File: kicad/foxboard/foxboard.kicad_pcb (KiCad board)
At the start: 2 copper layers, 356.7 x 159.4 mm, 183 parts, among them J2 USB_C_Receptacle_USB2.0, K1 KEYSW, K10 KEYSW, K11 KEYSW, K12 KEYSW, K13 KEYSW, K14 KEYSW, K15 KEYSW, K16 KEYSW, K17 KEYSW, K18 KEYSW, K19 KEYSW, K2 KEYSW, K20 KEYSW, K21 KEYSW, K22 KEYSW, K23 KEYSW, K24 KEYSW, K25 KEYSW, K26 KEYSW, K27 KEYSW, K28 KEYSW, K29 KEYSW, K3 KEYSW, K30 KEYSW, K31 KEYSW, K32 KEYSW, K33 KEYSW, K34 KEYSW, K35 KEYSW, K36 KEYSW, K37 KEYSW, K38 KEYSW, K39 KEYSW, K4 KEYSW, K40 KEYSW, K41 KEYSW, K42 KEYSW, K43 KEYSW, K44 KEYSW, K45 KEYSW, K46 KEYSW, K47 KEYSW, K48 KEYSW, K49 KEYSW, K5 KEYSW, K50 KEYSW, K51 KEYSW, K52 KEYSW, K53 KEYSW, K54 KEYSW, K55 KEYSW, K56 KEYSW, K57 KEYSW, K58 KEYSW, K59 KEYSW, K6 KEYSW, K60 KEYSW, K61 KEYSW, K62 KEYSW, K63 KEYSW, K64 KEYSW, K65 KEYSW, K66 KEYSW, K67 KEYSW, K68 KEYSW, K69 KEYSW, K7 KEYSW, K70 KEYSW, K71 KEYSW, K72 KEYSW, K73 KEYSW, K74 KEYSW, K75 KEYSW, K76 KEYSW, K77 KEYSW, K78 KEYSW, K79 KEYSW, K8 KEYSW, K80 KEYSW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

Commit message: move all resitors, caps and diodes to the back of the pcb
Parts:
- C3, C4, C5, C6, C7, D1, D10, D11, D12, D13, D14, D15, D16, D17, D18, D19, D2, D20, D22, D23, D24, D25, D26, D27, D28, D29, D3, D30, D31, D32, D33, D34, D35, D36, D37, D38, D39, D4, D40, D41, D42, D43, D44, D45, D46, D47, D48, D49, D5, D50, D51, D52, D53, D54, D55, D56, D57, D58, D59, D6, D60, D61, D62, D63, D64, D65, D66, D67, D68, D69, D7, D70, D71, D72, D73, D74, D75, D76, D77, D78, D79, D8, D80, D81, D82, D83, D84, D85, D86, D87, D9, R5, R6: moved to B.Cu
- moved D68 28.5 mm to (243.1, 259.5), turned to 180 degrees
- moved D87 23.4 mm to (272.5, 259.6), turned to 180 degrees
- moved D69 21.1 mm to (294.3, 259.6), turned to 180 degrees
- moved D54 20.4 mm to (315.0, 278.3), turned to 180 degrees
- moved D70 20.1 mm to (313.7, 259.7), turned to 180 degrees
- moved D52 19.9 mm to (277.4, 278.2), turned to 180 degrees
- moved D53 18.5 mm to (298.2, 278.3), turned to 180 degrees
- moved D58 16.7 mm to (48.5, 259.4), turned to 180 degrees
- moved D60 16.5 mm to (86.4, 259.3), turned to 180 degrees
- moved D65 16.5 mm to (182.8, 259.3), turned to 180 degrees
- moved D55 16.2 mm to (-8.40, 259.3), turned to 180 degrees
- moved D57 16.2 mm to (29.7, 259.4), turned to 180 degrees
- moved D59 16.2 mm to (68.0, 259.4), turned to 180 degrees
- moved D61 16.2 mm to (106.5, 259.4), turned to 180 degrees
- moved D56 16.0 mm to (11.0, 259.4), turned to 180 degrees
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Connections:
- K1 pad 1: Net-(K1-Pad1) -> Net-(U2-39_MISO1_OUT1A)
- K10 pad 1: Net-(K10-Pad1) -> Net-(U2-1_TX1_CTX2_MISO1)
- K11 pad 1: Net-(K11-Pad1) -> Net-(U2-0_RX1_CRX2_CS1)
- K13 pad 1: Net-(K13-Pad1) -> Net-(U2-40_A16)
- K14 pad 1: Net-(K14-Pad1) -> Net-(U2-41_A17)
- K15 pad 1: Net-(K15-Pad1) -> Net-(U2-13_SCK_LED)
- K16 pad 1: Net-(K16-Pad1) -> Net-(U2-14_A0_TX3_SPDIF_OUT)
- K17 pad 1: Net-(K17-Pad1) -> Net-(U2-15_A1_RX3_SPDIF_IN)
- K18 pad 1: Net-(K18-Pad1) -> Net-(U2-16_A2_RX4_SCL1)
- K19 pad 1: Net-(K19-Pad1) -> Net-(U2-17_A3_TX4_SDA1)
- K2 pad 1: Net-(K13-Pad1) -> Net-(U2-40_A16)
- K20 pad 1: Net-(K20-Pad1) -> Net-(U2-8_TX2_IN1)
- K21 pad 1: Net-(K21-Pad1) -> Net-(U2-7_RX2_OUT1A)
- K22 pad 1: Net-(K22-Pad1) -> Net-(U2-6_OUT1D)
- K24 pad 1: Net-(K10-Pad1) -> Net-(U2-1_TX1_CTX2_MISO1)
- K25 pad 1: Net-(K1-Pad1) -> Net-(U2-39_MISO1_OUT1A)
- K26 pad 1: Net-(K13-Pad1) -> Net-(U2-40_A16)
- K27 pad 1: Net-(K14-Pad1) -> Net-(U2-41_A17)
- K28 pad 1: Net-(K15-Pad1) -> Net-(U2-13_SCK_LED)
- K29 pad 1: Net-(K16-Pad1) -> Net-(U2-14_A0_TX3_SPDIF_OUT)
- K3 pad 1: Net-(K14-Pad1) -> Net-(U2-41_A17)
- K30 pad 1: Net-(K17-Pad1) -> Net-(U2-15_A1_RX3_SPDIF_IN)
- K31 pad 1: Net-(K18-Pad1) -> Net-(U2-16_A2_RX4_SCL1)
- K32 pad 1: Net-(K19-Pad1) -> Net-(U2-17_A3_TX4_SDA1)
- K33 pad 1: Net-(K20-Pad1) -> Net-(U2-8_TX2_IN1)
- K34 pad 1: Net-(K21-Pad1) -> Net-(U2-7_RX2_OUT1A)
- K35 pad 1: Net-(K22-Pad1) -> Net-(U2-6_OUT1D)
- K38 pad 1: Net-(K13-Pad1) -> Net-(U2-40_A16)
- K39 pad 1: Net-(K14-Pad1) -> Net-(U2-41_A17)
- K40 pad 1: Net-(K15-Pad1) -> Net-(U2-13_SCK_LED)
- K41 pad 1: Net-(K16-Pad1) -> Net-(U2-14_A0_TX3_SPDIF_OUT)
- K42 pad 1: Net-(K17-Pad1) -> Net-(U2-15_A1_RX3_SPDIF_IN)
- K43 pad 1: Net-(K18-Pad1) -> Net-(U2-16_A2_RX4_SCL1)
- K44 pad 1: Net-(K19-Pad1) -> Net-(U2-17_A3_TX4_SDA1)
- K45 pad 1: Net-(K20-Pad1) -> Net-(U2-8_TX2_IN1)
- K46 pad 1: Net-(K21-Pad1) -> Net-(U2-7_RX2_OUT1A)
- K48 pad 1: Net-(K22-Pad1) -> Net-(U2-6_OUT1D)
- K5 pad 1: Net-(K20-Pad1) -> Net-(U2-8_TX2_IN1)
- K51 pad 1: Net-(K51-Pad1) -> Net-(U2-2_OUT2)
- K52 pad 1: Net-(K10-Pad1) -> Net-(U2-1_TX1_CTX2_MISO1)
- K53 pad 1: Net-(K11-Pad1) -> Net-(U2-0_RX1_CRX2_CS1)
- K54 pad 1: Net-(K1-Pad1) -> Net-(U2-39_MISO1_OUT1A)
- K55 pad 1: Net-(K13-Pad1) -> Net-(U2-40_A16)
- K56 pad 1: Net-(K14-Pad1) -> Net-(U2-41_A17)
- K57 pad 1: Net-(K15-Pad1) -> Net-(U2-13_SCK_LED)
- K58 pad 1: Net-(K16-Pad1) -> Net-(U2-14_A0_TX3_SPDIF_OUT)
- K59 pad 1: Net-(K17-Pad1) -> Net-(U2-15_A1_RX3_SPDIF_IN)
- K6 pad 1: Net-(K21-Pad1) -> Net-(U2-7_RX2_OUT1A)
- K60 pad 1: Net-(K18-Pad1) -> Net-(U2-16_A2_RX4_SCL1)
- K61 pad 1: Net-(K19-Pad1) -> Net-(U2-17_A3_TX4_SDA1)
- K62 pad 1: Net-(K20-Pad1) -> Net-(U2-8_TX2_IN1)
- K63 pad 1: Net-(K21-Pad1) -> Net-(U2-7_RX2_OUT1A)
- K65 pad 1: Net-(K22-Pad1) -> Net-(U2-6_OUT1D)
- K68 pad 1: Net-(K68-Pad1) -> Net-(U2-3_LRCLK2)
- K7 pad 1: Net-(K22-Pad1) -> Net-(U2-6_OUT1D)
- K70 pad 1: Net-(K11-Pad1) -> Net-(U2-0_RX1_CRX2_CS1)
- K71 pad 1: Net-(K1-Pad1) -> Net-(U2-39_MISO1_OUT1A)
- K72 pad 1: Net-(K13-Pad1) -> Net-(U2-40_A16)
- K73 pad 1: Net-(K14-Pad1) -> Net-(U2-41_A17)
- K74 pad 1: Net-(K16-Pad1) -> Net-(U2-14_A0_TX3_SPDIF_OUT)
- K75 pad 1: Net-(K17-Pad1) -> Net-(U2-15_A1_RX3_SPDIF_IN)
- K76 pad 1: Net-(K18-Pad1) -> Net-(U2-16_A2_RX4_SCL1)
- K77 pad 1: Net-(K19-Pad1) -> Net-(U2-17_A3_TX4_SDA1)
- K78 pad 1: Net-(K20-Pad1) -> Net-(U2-8_TX2_IN1)
- K79 pad 1: Net-(K21-Pad1) -> Net-(U2-7_RX2_OUT1A)
- K80 pad 1: Net-(K22-Pad1) -> Net-(U2-6_OUT1D)
- K81 pad 1: unconnected-(K81-Pad1) -> Net-(U2-5_IN2)
- K82 pad 1: unconnected-(K82-Pad1) -> Net-(U2-4_BCLK2)
- K83 pad 1: Net-(K68-Pad1) -> Net-(U2-3_LRCLK2)
- K84 pad 1: Net-(K51-Pad1) -> Net-(U2-2_OUT2)
- K85 pad 1: Net-(K10-Pad1) -> Net-(U2-1_TX1_CTX2_MISO1)
- K86 pad 1: Net-(K11-Pad1) -> Net-(U2-0_RX1_CRX2_CS1)
- K87 pad 1: Net-(K51-Pad1) -> Net-(U2-2_OUT2)
- K9 pad 1: Net-(K51-Pad1) -> Net-(U2-2_OUT2)
- U2 pad 10: unconnected-(U2-8_TX2_IN1-Pad10) -> Net-(U2-8_TX2_IN1)
- U2 pad 2: unconnected-(U2-0_RX1_CRX2_CS1-Pad2) -> Net-(U2-0_RX1_CRX2_CS1)
- U2 pad 25: unconnected-(U2-33_MCLK2-Pad25) -> Net-(D1-K)
- U2 pad 26: unconnected-(U2-34_RX8-Pad26) -> Net-(D12-K)
- U2 pad 27: unconnected-(U2-35_TX8-Pad27) -> Net-(D25-K)
- U2 pad 28: unconnected-(U2-36_CS-Pad28) -> Net-(D37-K)
- U2 pad 29: unconnected-(U2-37_CS-Pad29) -> Net-(D54-K)
- U2 pad 3: unconnected-(U2-1_TX1_CTX2_MISO1-Pad3) -> Net-(U2-1_TX1_CTX2_MISO1)
- U2 pad 30: unconnected-(U2-38_CS1_IN1-Pad30) -> Net-(D71-K)
- U2 pad 31: unconnected-(U2-39_MISO1_OUT1A-Pad31) -> Net-(U2-39_MISO1_OUT1A)
- U2 pad 32: unconnected-(U2-40_A16-Pad32) -> Net-(U2-40_A16)
- U2 pad 33: unconnected-(U2-41_A17-Pad33) -> Net-(U2-41_A17)
- U2 pad 35: unconnected-(U2-13_SCK_LED-Pad35) -> Net-(U2-13_SCK_LED)
- U2 pad 36: unconnected-(U2-14_A0_TX3_SPDIF_OUT-Pad36) -> Net-(U2-14_A0_TX3_SPDIF_OUT)
- U2 pad 37: unconnected-(U2-15_A1_RX3_SPDIF_IN-Pad37) -> Net-(U2-15_A1_RX3_SPDIF_IN)
- U2 pad 38: unconnected-(U2-16_A2_RX4_SCL1-Pad38) -> Net-(U2-16_A2_RX4_SCL1)
- U2 pad 39: unconnected-(U2-17_A3_TX4_SDA1-Pad39) -> Net-(U2-17_A3_TX4_SDA1)
- U2 pad 4: unconnected-(U2-2_OUT2-Pad4) -> Net-(U2-2_OUT2)
- U2 pad 5: unconnected-(U2-3_LRCLK2-Pad5) -> Net-(U2-3_LRCLK2)
- U2 pad 6: unconnected-(U2-4_BCLK2-Pad6) -> Net-(U2-4_BCLK2)
- U2 pad 7: unconnected-(U2-5_IN2-Pad7) -> Net-(U2-5_IN2)
- U2 pad 8: unconnected-(U2-6_OUT1D-Pad8) -> Net-(U2-6_OUT1D)
- U2 pad 9: unconnected-(U2-7_RX2_OUT1A-Pad9) -> Net-(U2-7_RX2_OUT1A)
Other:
- board size 356.7 x 159.4 mm -> 356.7 x 154.4 mm

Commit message: update footprint to be 1.5u
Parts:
- K51: footprint PCM_marbastlib-mx:SW_MX_1.25u -> PCM_marbastlib-mx:SW_MX_1.5u
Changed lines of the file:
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@@
       (net 85 "Net-(D77-A)") (pintype "passive"))
   )
-  (footprint "PCM_marbastlib-mx:SW_MX_1.25u" (layer "F.Cu")
-    (at 248.08785 286.9726)
+  (footprint "PCM_marbastlib-mx:SW_MX_1.5u" (layer "F.Cu")
+    (at 248.08785 287.02)
     (descr "Footprint for Cherry MX style switches")
     (property "Sheetfile" "foxboard.kicad_sch")
     (property "Sheetname" "")
-    (attr through_hole exclude_from_pos_files)
+    (attr through_hole exclude_from_pos_files exclude_from_bom)
     (fp_text reference "K51" (at 0 3.175) (layer "Dwgs.User") hide
         (effects (font (size 1 1) (thickness 0.15)))
@@
         (effects (font (size 1 1) (thickness 0.15)))
     )
-    (fp_line (start -11.90625 -9.525) (end -11.90625 9.525)
+    (fp_line (start -14.2875 -9.525) (end -14.2875 9.525)
       (stroke (width 0.12) (type solid)) (layer "Dwgs.User"))
-    (fp_line (start -11.90625 9.525) (end 11.90625 9.525)
+    (fp_line (start -14.2875 9.525) (end 14.2875 9.525)
       (stroke (width 0.12) (type solid)) (layer "Dwgs.User"))
-    (fp_line (start 11.90625 -9.525) (end -11.90625 -9.525)
+    (fp_line (start 14.2875 -9.525) (end -14.2875 -9.525)
       (stroke (width 0.12) (type solid)) (layer "Dwgs.User"))
-    (fp_line (start 11.90625 9.525) (end 11.90625 -9.525)
+    (fp_line (start 14.2875 9.525) (end 14.2875 -9.525)
       (stroke (width 0.12) (type solid)) (layer "Dwgs.User"))
     (fp_line (start -7 6.5) (end -7 -6.5)

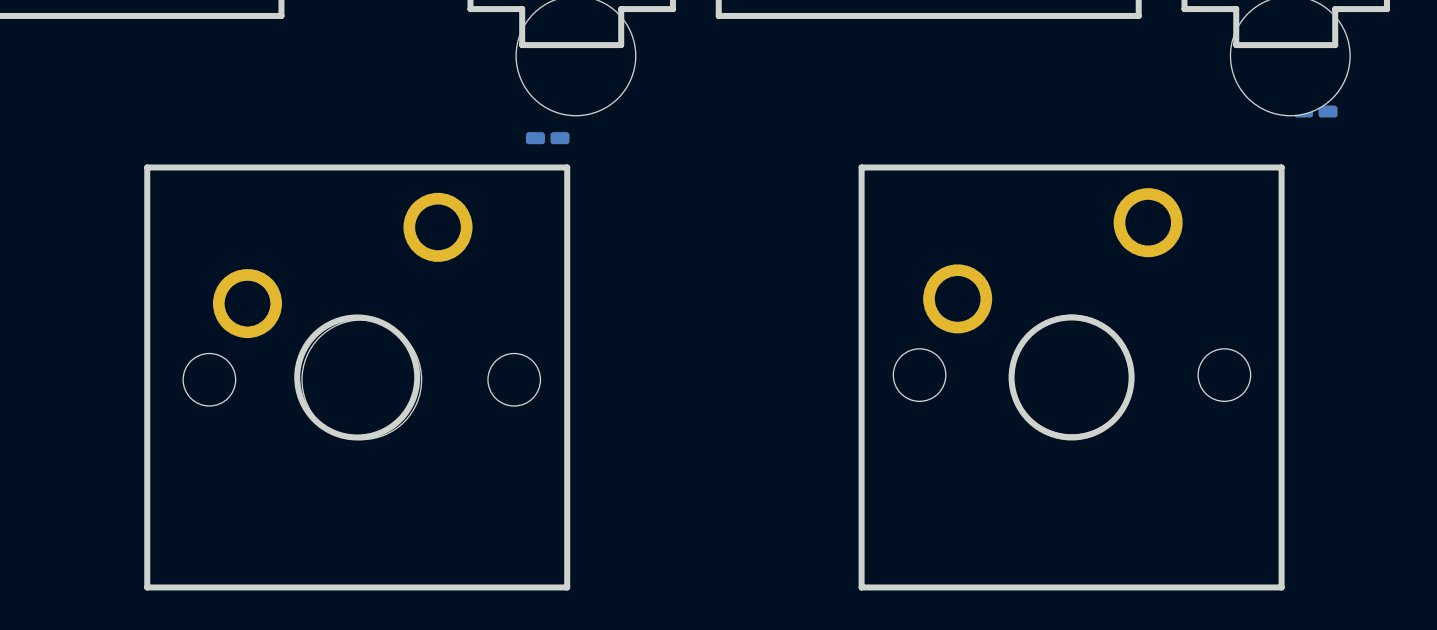
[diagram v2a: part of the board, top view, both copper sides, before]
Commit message: move a keyswitch
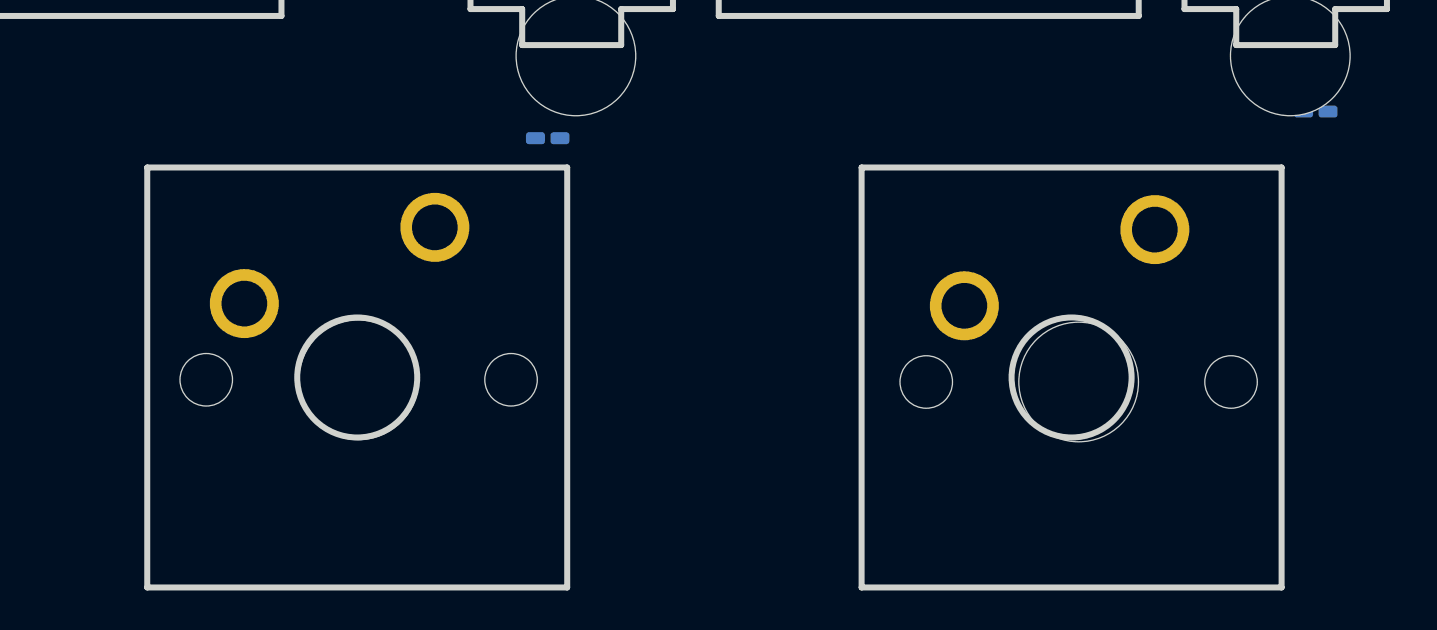
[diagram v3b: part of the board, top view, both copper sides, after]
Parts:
- moved K51 0.32 mm to (248.3, 287.2)
- moved K50 0.11 mm to (224.3, 287.2)
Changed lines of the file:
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@@
   )
   (footprint "PCM_marbastlib-mx:SW_MX_1u" (layer "F.Cu")
-    (at 224.41505 287.1758)
+    (at 224.31 287.1758)
     (descr "Footprint for Cherry MX style switches")
     (tags "cherry mx switch")
@@
   )
   (footprint "PCM_marbastlib-mx:SW_MX_1.5u" (layer "F.Cu")
-    (at 248.08785 287.02)
-    (descr "Footprint for Cherry MX style switches")
-    (property "Sheetfile" "foxboard.kicad_sch")
+    (at 248.31 287.25)
+    (descr "Footprint for Cherry MX style switches")
+    (property "Sheetfile" "foxboard.kicad_sch")

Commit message: flip diode that was missing
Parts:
- D21: moved to B.Cu
- turned D21 to 180 degrees
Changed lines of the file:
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@@
       (net 41 "Net-(D36-A)") (pintype "passive"))
   )
-  (footprint "Diode_SMD:D_0201_0603Metric_Pad0.64x0.40mm_HandSolder" (layer "F.Cu")
-    (at 189.33765 316.9446)
-    (descr "Diode SMD 0201 (0603 Metric), square (rectangular) end terminal, IPC_7351 nominal, (Body size source: https://www.vishay.com/docs/20052/crcw0201e3.pdf), generated with kicad-footprint-generator")
-    (tags "diode handsolder")
-    (property "Sheetfile" "foxboard.kicad_sch")
-    (property "Sheetname" "")
-    (property "Sim.Device" "D")
-    (property "Sim.Pins" "1=K 2=A")
-    (property "ki_description" "Diode")
-    (property "ki_keywords" "diode")
-    (attr smd)
-    (fp_text reference "D21" (at 0 -1.05) (layer "F.SilkS")
-        (effects (font (size 1 1) (thickness 0.15)))
-    )
-    (fp_text value "D" (at 0 1.05) (layer "F.Fab")
-        (effects (font (size 1 1) (thickness 0.15)))
-    )
-    (fp_text user "${REFERENCE}" (at 0 -0.68) (layer "F.Fab")
-        (effects (font (size 0.25 0.25) (thickness 0.04)))
-    )
-    (fp_circle (center -1.035 0) (end -0.985 0)
-      (stroke (width 0.1) (type solid)) (fill none) (layer "F.SilkS"))
-    (fp_line (start -0.88 -0.35) (end 0.88 -0.35)
-      (stroke (width 0.05) (type solid)) (layer "F.CrtYd"))
-    (fp_line (start -0.88 0.35) (end -0.88 -0.35)
-      (stroke (width 0.05) (type solid)) (layer "F.CrtYd"))
-    (fp_line (start 0.88 -0.35) (end 0.88 0.35)
-      (stroke (width 0.05) (type solid)) (layer "F.CrtYd"))
-    (fp_line (start 0.88 0.35) (end -0.88 0.35)
-      (stroke (width 0.05) (type solid)) (layer "F.CrtYd"))
-    (fp_line (start -0.3 -0.15) (end 0.3 -0.15)
-      (stroke (width 0.1) (type solid)) (layer "F.Fab"))
-    (fp_line (start -0.3 0.15) (end -0.3 -0.15)
-      (stroke (width 0.1) (type solid)) (layer "F.Fab"))
-    (fp_line (start -0.2 0.15) (end -0.2 -0.15)
-      (stroke (width 0.1) (type solid)) (layer "F.Fab"))
-    (fp_line (start -0.1 0.15) (end -0.1 -0.15)
-      (stroke (width 0.1) (type solid)) (layer "F.Fab"))
-    (fp_line (start 0.3 -0.15) (end 0.3 0.15)
-      (stroke (width 0.1) (type solid)) (layer "F.Fab"))
-    (fp_line (start 0.3 0.15) (end -0.3 0.15)
-      (stroke (width 0.1) (type solid)) (layer "F.Fab"))
-    (pad "" smd roundrect (at -0.4325 0) (size 0.458 0.36) (layers "F.Paste") (roundrect_rratio 0.25))
-    (pad "" smd roundrect (at 0.4325 0) (size 0.458 0.36) (layers "F.Paste") (roundrect_rratio 0.25))
-    (pad "1" smd roundrect (at -0.4075 0) (size 0.635 0.4) (layers "F.Cu" "F.Mask") (roundrect_rratio 0.25)
-      (net 15 "Net-(D12-K)") (pinfunction "K") (pintype "passive"))
-    (pad "2" smd roundrect (at 0.4075 0) (size 0.635 0.4) (layers "F.Cu" "F.Mask") (roundrect_rratio 0.25)
-      (net 25 "Net-(D21-A)") (pinfunction "A") (pintype "passive"))
-    (model "${KICAD6_3DMODEL_DIR}/Diode_SMD.3dshapes/D_0201_0603Metric.wrl"
-      (offset (xyz 0 0 0))
-      (scale (xyz 1 1 1))
-      (rotate (xyz 0 0 0))
-    )
-  )
   (footprint "PCM_marbastlib-mx:SW_MX_1u" (layer "F.Cu")
     (at 114.63625 306.2004)
@@
     (model "${KICAD6_3DMODEL_DIR}/Diode_SMD.3dshapes/D_0201_0603Metric.wrl"
       (offset (xyz 0 0 0))
+      (scale (xyz 1 1 1))
+      (rotate (xyz 0 0 0))
+    )
+  )
+  (footprint "Diode_SMD:D_0201_0603Metric_Pad0.64x0.40mm_HandSolder" (layer "B.Cu")
+    (at 189.33765 316.9446 180)
+    (descr "Diode SMD 0201 (0603 Metric), square (rectangular) end terminal, IPC_7351 nominal, (Body size source: https://www.vishay.com/docs/20052/crcw0201e3.pdf), generated with kicad-footprint-generator")
+    (tags "diode handsolder")
+    (property "Sheetfile" "foxboard.kicad_sch")
+    (property "Sheetname" "")
+    (property "Sim.Device" "D")
+    (property "Sim.Pins" "1=K 2=A")
+    (property "ki_description" "Diode")
+    (property "ki_keywords" "diode")
+    (attr smd)
+    (fp_text reference "D21" (at 0 1.05) (layer "B.SilkS")
+        (effects (font (size 1 1) (thickness 0.15)) (justify mirror))
+    )
+    (fp_text value "D" (at 0 -1.05) (layer "B.Fab")
+        (effects (font (size 1 1) (thickness 0.15)) (justify mirror))
+    )
+    (fp_text user "${REFERENCE}" (at 0 0.68) (layer "B.Fab")
+        (effects (font (size 0.25 0.25) (thickness 0.04)) (justify mirror))
+    )
+    (fp_circle (center -1.035 0) (end -0.985 0)
+      (stroke (width 0.1) (type solid)) (fill none) (layer "B.SilkS"))
+    (fp_line (start -0.88 -0.35) (end -0.88 0.35)
+      (stroke (width 0.05) (type solid)) (layer "B.CrtYd"))
+    (fp_line (start -0.88 0.35) (end 0.88 0.35)
+      (stroke (width 0.05) (type solid)) (layer "B.CrtYd"))
+    (fp_line (start 0.88 -0.35) (end -0.88 -0.35)
+      (stroke (width 0.05) (type solid)) (layer "B.CrtYd"))
+    (fp_line (start 0.88 0.35) (end 0.88 -0.35)
+      (stroke (width 0.05) (type solid)) (layer "B.CrtYd"))
+    (fp_line (start -0.3 -0.15) (end -0.3 0.15)
+      (stroke (width 0.1) (type solid)) (layer "B.Fab"))
+    (fp_line (start -0.3 0.15) (end 0.3 0.15)
+      (stroke (width 0.1) (type solid)) (layer "B.Fab"))
+    (fp_line (start -0.2 -0.15) (end -0.2 0.15)
+      (stroke (width 0.1) (type solid)) (layer "B.Fab"))
+    (fp_line (start -0.1 -0.15) (end -0.1 0.15)
+      (stroke (width 0.1) (type solid)) (layer "B.Fab"))
+    (fp_line (start 0.3 -0.15) (end -0.3 -0.15)
+      (stroke (width 0.1) (type solid)) (layer "B.Fab"))
+    (fp_line (start 0.3 0.15) (end 0.3 -0.15)
+      (stroke (width 0.1) (type solid)) (layer "B.Fab"))
+    (pad "" smd roundrect (at -0.4325 0 180) (size 0.458 0.36) (layers "B.Paste") (roundrect_rratio 0.25))
+    (pad "" smd roundrect (at 0.4325 0 180) (size 0.458 0.36) (layers "B.Paste") (roundrect_rratio 0.25))
+    (pad "1" smd roundrect (at -0.4075 0 180) (size 0.635 0.4) (layers "B.Cu" "B.Mask") (roundrect_rratio 0.25)
+      (net 15 "Net-(D12-K)") (pinfunction "K") (pintype "passive"))
+    (pad "2" smd roundrect (at 0.4075 0 180) (size 0.635 0.4) (layers "B.Cu" "B.Mask") (roundrect_rratio 0.25)
+      (net 25 "Net-(D21-A)") (pinfunction "A") (pintype "passive"))
+    (model "${KICAD6_3DMODEL_DIR}/Diode_SMD.3dshapes/D_0201_0603Metric.wrl"
+      (offset (xyz 0 0 0))

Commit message: reimported keyboard-layout.dxf as Foreground Silk Layer
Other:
- board size 356.7 x 154.4 mm -> 40.2 x 15 mm

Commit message: update footprints
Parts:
- added REF**: STAB_MX_6.25u, PCM_marbastlib-mx:STAB_MX_6.25u, F.Cu at (106.7, 342.9)
- K12: footprint PCM_marbastlib-mx:STAB_MX_2.25u -> PCM_marbastlib-xp-plate-mx:Plate_MX_SPLIT-RSHIFT
- K25: footprint PCM_marbastlib-mx:SW_MX_HS_1.75u -> PCM_marbastlib-mx:STAB_MX_2.25u
- K37: footprint PCM_marbastlib-mx:STAB_MX_2u -> PCM_marbastlib-mx:STAB_MX_ISO
- K38, K51: footprint PCM_marbastlib-mx:SW_MX_1.5u -> PCM_marbastlib-mx:SW_MX_1.75u
- K4: footprint Mounting_Keyboard_Stabilizer:Stabilizer_Cherry_MX_6.25u -> rhais_cherry:MX_KEY_4.45
- K69: footprint PCM_marbastlib-mx:STAB_MX_2u -> PCM_marbastlib-mx:STAB_MX_2.75u
- moved D4 65.2 mm to (135.1, 336.0)
- moved J2 10.1 mm to (5.08, 223.5), turned to 180 degrees
- moved K12 3.16 mm to (-5.08, 325.3)
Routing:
- net Net-(D4-A): track 0.00 -> 25.8 mm
- net Net-(D2-A): track 0.00 -> 8.28 mm
- net Net-(D3-A): track 0.00 -> 7.73 mm
- net Net-(D1-A): track 0.00 -> 7.10 mm
